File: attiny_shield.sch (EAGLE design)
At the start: 10 parts, among them IC1 TINY13-20PU

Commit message: reset pins won't need to be set manually
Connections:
- removed net 84_RESET: J3.4, U$1.(PCINT11/~RESET/DW)PB3
- removed net 85_RESET: IC1.PB5/PCINT5/!RESET!/ADC0/DW, J4.1
- removed net RESET: U$2.D10
- new net TINY_RESET: IC1.PB5/PCINT5/!RESET!/ADC0/DW, J3.4, J4.1, U$1.(PCINT11/~RESET/DW)PB3, U$2.D10
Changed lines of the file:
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@@
 </segment>
 </net>
-<net name="RESET" class="0">
+<net name="TINY_RESET" class="0">
 <segment>
 <pinref part="U$2" gate="G$1" pin="D10"/>
 <wire x1="55.88" y1="147.32" x2="55.88" y2="152.4" width="0.1524" layer="91"/>
 <label x="55.88" y="149.86" size="1.778" layer="95"/>
+</segment>
+<segment>
+<pinref part="J4" gate="G$1" pin="1"/>
+<wire x1="144.78" y1="91.44" x2="134.62" y2="91.44" width="0.1524" layer="91"/>
+<label x="134.62" y="91.44" size="1.778" layer="95"/>
+</segment>
+<segment>
+<pinref part="IC1" gate="G$1" pin="PB5/PCINT5/!RESET!/ADC0/DW"/>
+<wire x1="121.92" y1="109.22" x2="147.32" y2="109.22" width="0.1524" layer="91"/>
+<label x="121.92" y="109.22" size="1.778" layer="95"/>
+</segment>
+<segment>
+<pinref part="J3" gate="G$1" pin="4"/>
+<wire x1="63.5" y1="22.86" x2="53.34" y2="22.86" width="0.1524" layer="91"/>
+<label x="53.34" y="22.86" size="1.778" layer="95"/>
+</segment>
+<segment>
+<pinref part="U$1" gate="G$1" pin="(PCINT11/~RESET/DW)PB3"/>
+<wire x1="30.48" y1="66.04" x2="20.32" y2="66.04" width="0.1524" layer="91"/>
+<label x="22.86" y="66.04" size="1.778" layer="95"/>
 </segment>
 </net>
@@
 </segment>
 </net>
-<net name="84_RESET" class="0">
-<segment>
-<pinref part="J3" gate="G$1" pin="4"/>
-<wire x1="63.5" y1="22.86" x2="53.34" y2="22.86" width="0.1524" layer="91"/>
-<label x="53.34" y="22.86" size="1.778" layer="95"/>
-</segment>
-<segment>
-<pinref part="U$1" gate="G$1" pin="(PCINT11/~RESET/DW)PB3"/>
-<wire x1="30.48" y1="66.04" x2="20.32" y2="66.04" width="0.1524" layer="91"/>
-<label x="22.86" y="66.04" size="1.778" layer="95"/>
-</segment>
-</net>
-<net name="85_RESET" class="0">
-<segment>
-<pinref part="J4" gate="G$1" pin="1"/>
-<wire x1="144.78" y1="91.44" x2="134.62" y2="91.44" width="0.1524" layer="91"/>
-<label x="134.62" y="91.44" size="1.778" layer="95"/>
-</segment>
-<segment>
-<pinref part="IC1" gate="G$1" pin="PB5/PCINT5/!RESET!/ADC0/DW"/>
-<wire x1="121.92" y1="109.22" x2="147.32" y2="109.22" width="0.1524" layer="91"/>
-<label x="121.92" y="109.22" size="1.778" layer="95"/>
-</segment>
-</net>

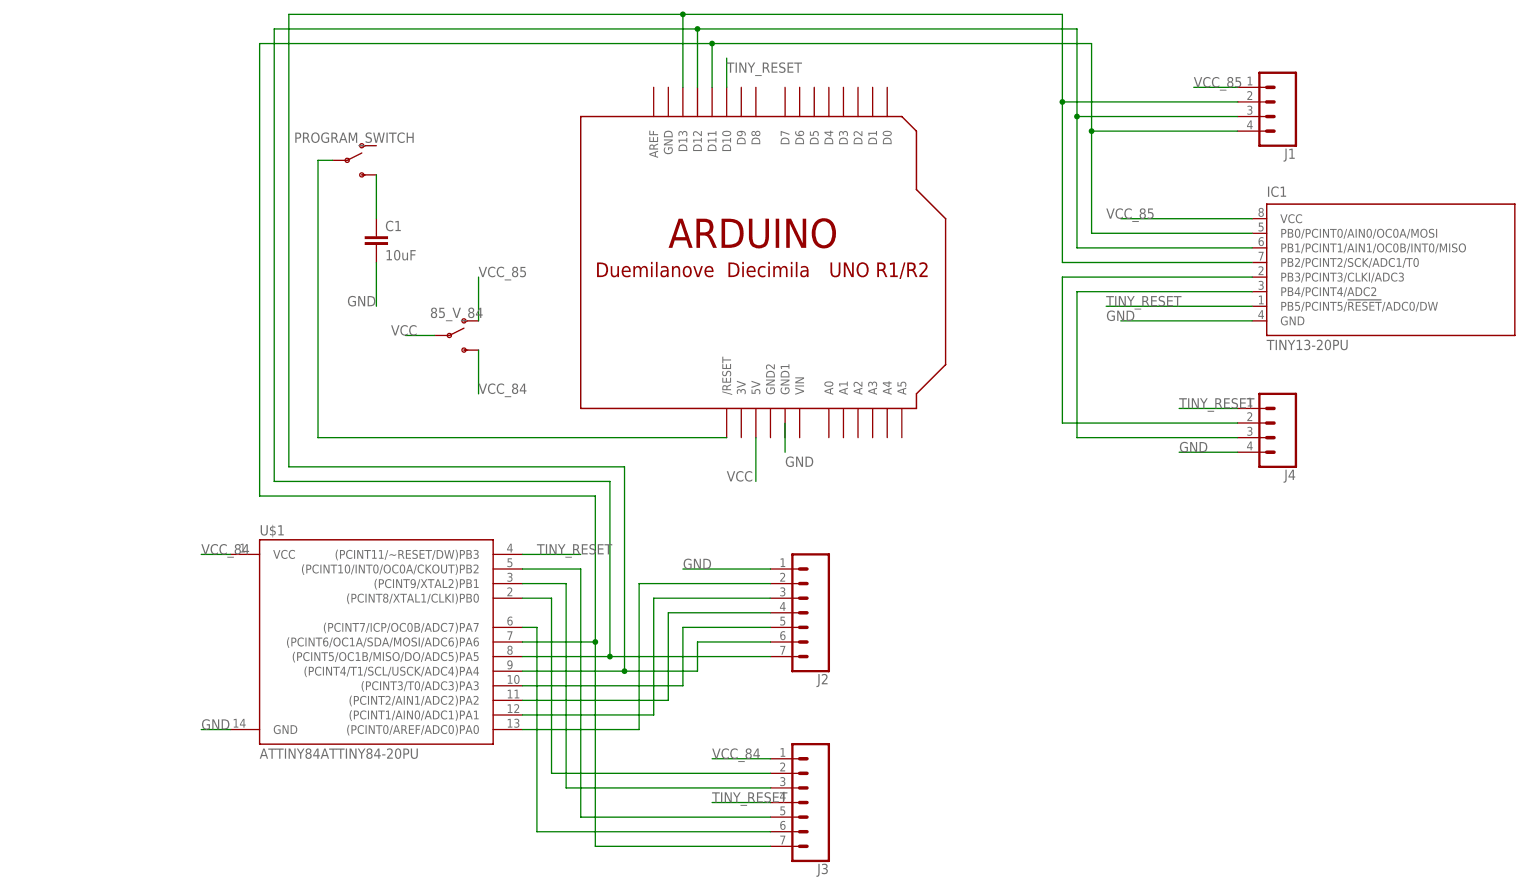
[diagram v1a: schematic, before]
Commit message: reset not vcc
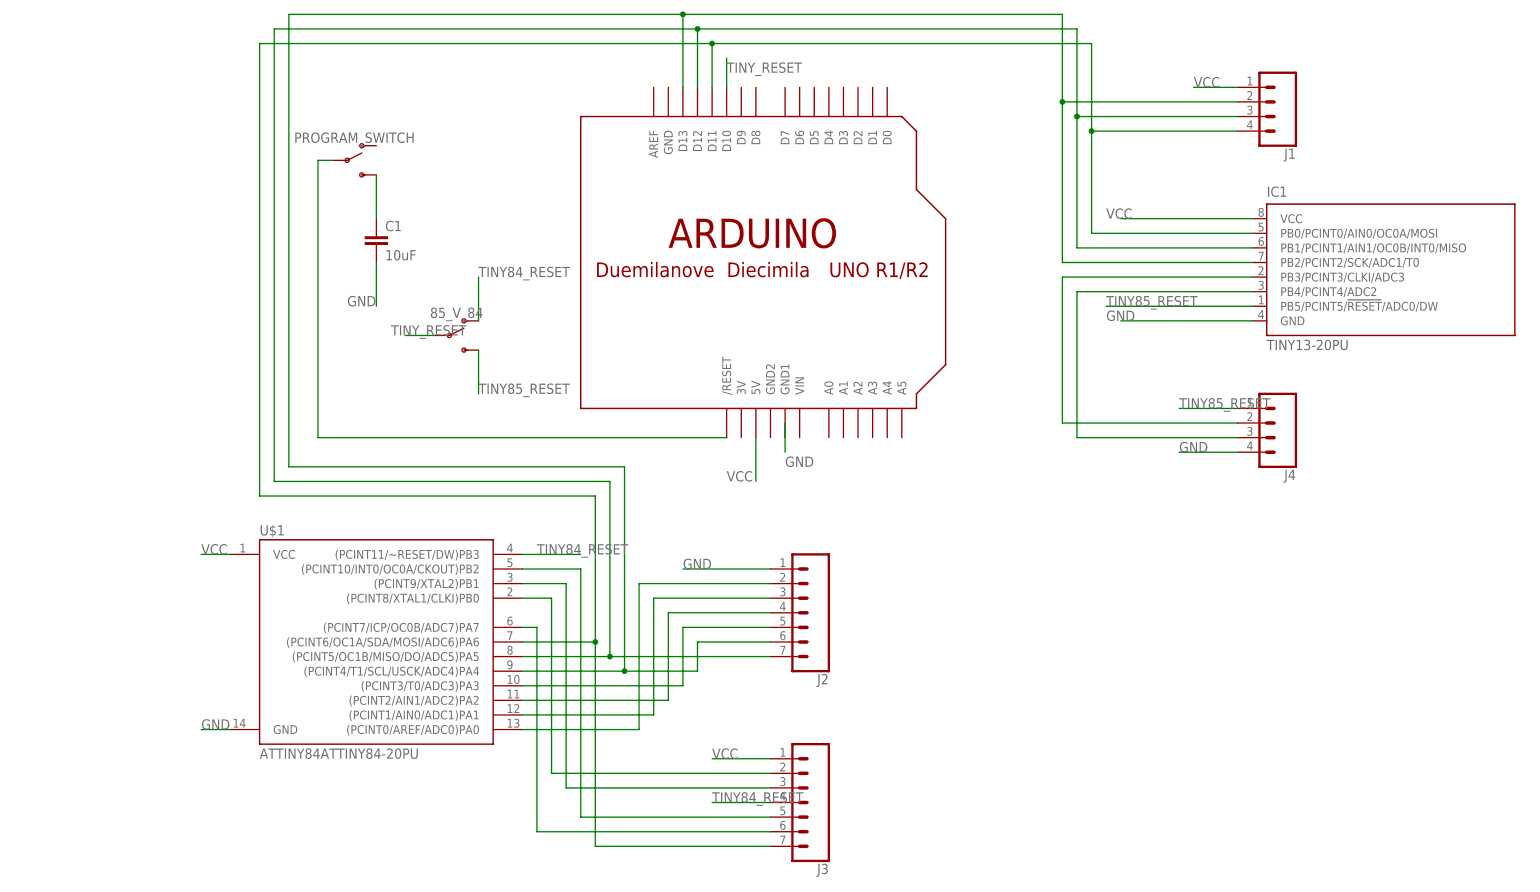
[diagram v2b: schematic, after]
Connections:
- removed net VCC_84: 85_V_84.S, J3.1, U$1.VCC
- removed net VCC_85: 85_V_84.O, IC1.VCC, J1.1
- new net TINY84_RESET: 85_V_84.O, J3.4, U$1.(PCINT11/~RESET/DW)PB3
- new net TINY85_RESET: 85_V_84.S, IC1.PB5/PCINT5/!RESET!/ADC0/DW, J4.1
- net TINY_RESET: now also 85_V_84.P; no longer IC1.PB5/PCINT5/!RESET!/ADC0/DW, J3.4, J4.1, U$1.(PCINT11/~RESET/DW)PB3
- net VCC: now also IC1.VCC, J1.1, J3.1, U$1.VCC; no longer 85_V_84.P
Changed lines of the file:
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@@
 </segment>
 <segment>
-<pinref part="J4" gate="G$1" pin="1"/>
-<wire x1="144.78" y1="91.44" x2="134.62" y2="91.44" width="0.1524" layer="91"/>
-<label x="134.62" y="91.44" size="1.778" layer="95"/>
-</segment>
-<segment>
-<pinref part="IC1" gate="G$1" pin="PB5/PCINT5/!RESET!/ADC0/DW"/>
-<wire x1="121.92" y1="109.22" x2="147.32" y2="109.22" width="0.1524" layer="91"/>
-<label x="121.92" y="109.22" size="1.778" layer="95"/>
-</segment>
-<segment>
-<pinref part="J3" gate="G$1" pin="4"/>
-<wire x1="63.5" y1="22.86" x2="53.34" y2="22.86" width="0.1524" layer="91"/>
-<label x="53.34" y="22.86" size="1.778" layer="95"/>
-</segment>
-<segment>
-<pinref part="U$1" gate="G$1" pin="(PCINT11/~RESET/DW)PB3"/>
-<wire x1="30.48" y1="66.04" x2="20.32" y2="66.04" width="0.1524" layer="91"/>
-<label x="22.86" y="66.04" size="1.778" layer="95"/>
-</segment>
-</net>
-<net name="VCC_85" class="0">
-<segment>
-<pinref part="85_V_84" gate="1" pin="O"/>
-<wire x1="12.7" y1="106.68" x2="12.7" y2="114.3" width="0.1524" layer="91"/>
-<label x="12.7" y="114.3" size="1.778" layer="95"/>
-</segment>
-<segment>
-<pinref part="IC1" gate="G$1" pin="VCC"/>
-<wire x1="147.32" y1="124.46" x2="124.46" y2="124.46" width="0.1524" layer="91"/>
-<label x="121.92" y="124.46" size="1.778" layer="95"/>
-</segment>
-<segment>
-<pinref part="J1" gate="G$1" pin="1"/>
-<wire x1="144.78" y1="147.32" x2="137.16" y2="147.32" width="0.1524" layer="91"/>
-<label x="137.16" y="147.32" size="1.778" layer="95"/>
+<pinref part="85_V_84" gate="1" pin="P"/>
+<wire x1="5.08" y1="104.14" x2="0" y2="104.14" width="0.1524" layer="91"/>
+<label x="-2.54" y="104.14" size="1.778" layer="95"/>
 </segment>
 </net>
@@
 </segment>
 <segment>
-<pinref part="85_V_84" gate="1" pin="P"/>
-<wire x1="5.08" y1="104.14" x2="0" y2="104.14" width="0.1524" layer="91"/>
-<label x="-2.54" y="104.14" size="1.778" layer="95"/>
-</segment>
-</net>
-<net name="VCC_84" class="0">
-<segment>
 <pinref part="U$1" gate="G$1" pin="VCC"/>
 <wire x1="-35.56" y1="66.04" x2="-30.48" y2="66.04" width="0.1524" layer="91"/>
@@
 </segment>
 <segment>
-<pinref part="85_V_84" gate="1" pin="S"/>
-<wire x1="12.7" y1="101.6" x2="12.7" y2="93.98" width="0.1524" layer="91"/>
-<label x="12.7" y="93.98" size="1.778" layer="95"/>
-</segment>
-<segment>
 <pinref part="J3" gate="G$1" pin="1"/>
 <wire x1="63.5" y1="30.48" x2="53.34" y2="30.48" width="0.1524" layer="91"/>
 <label x="53.34" y="30.48" size="1.778" layer="95"/>
+</segment>
+<segment>
+<pinref part="IC1" gate="G$1" pin="VCC"/>
+<wire x1="147.32" y1="124.46" x2="124.46" y2="124.46" width="0.1524" layer="91"/>
+<label x="121.92" y="124.46" size="1.778" layer="95"/>
+</segment>
+<segment>
+<pinref part="J1" gate="G$1" pin="1"/>
+<wire x1="144.78" y1="147.32" x2="137.16" y2="147.32" width="0.1524" layer="91"/>
+<label x="137.16" y="147.32" size="1.778" layer="95"/>
 </segment>
 </net>
@@
 </segment>
 </net>
+<net name="TINY85_RESET" class="0">
+<segment>
+<pinref part="IC1" gate="G$1" pin="PB5/PCINT5/!RESET!/ADC0/DW"/>
+<wire x1="121.92" y1="109.22" x2="147.32" y2="109.22" width="0.1524" layer="91"/>
+<label x="121.92" y="109.22" size="1.778" layer="95"/>
+</segment>
+<segment>
+<pinref part="J4" gate="G$1" pin="1"/>
+<wire x1="144.78" y1="91.44" x2="134.62" y2="91.44" width="0.1524" layer="91"/>
+<label x="134.62" y="91.44" size="1.778" layer="95"/>
+</segment>
+<segment>
+<pinref part="85_V_84" gate="1" pin="S"/>
+<wire x1="12.7" y1="101.6" x2="12.7" y2="93.98" width="0.1524" layer="91"/>
+<label x="12.7" y="93.98" size="1.778" layer="95"/>
+</segment>
+</net>
+<net name="TINY84_RESET" class="0">
+<segment>
+<pinref part="J3" gate="G$1" pin="4"/>
+<wire x1="63.5" y1="22.86" x2="53.34" y2="22.86" width="0.1524" layer="91"/>
+<label x="53.34" y="22.86" size="1.778" layer="95"/>
+</segment>
+<segment>
+<pinref part="U$1" gate="G$1" pin="(PCINT11/~RESET/DW)PB3"/>
+<wire x1="30.48" y1="66.04" x2="20.32" y2="66.04" width="0.1524" layer="91"/>
+<label x="22.86" y="66.04" size="1.778" layer="95"/>
+</segment>
+<segment>
+<pinref part="85_V_84" gate="1" pin="O"/>
+<wire x1="12.7" y1="106.68" x2="12.7" y2="114.3" width="0.1524" layer="91"/>
+<label x="12.7" y="114.3" size="1.778" layer="95"/>
+</segment>
+</net>

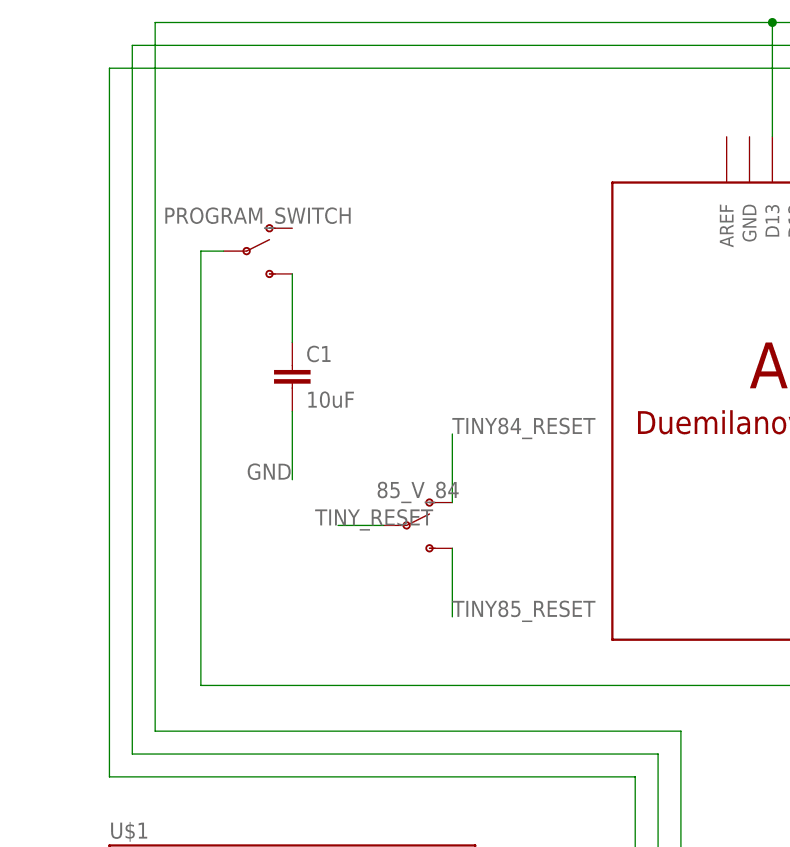
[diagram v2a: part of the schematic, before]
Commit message: added reset switch
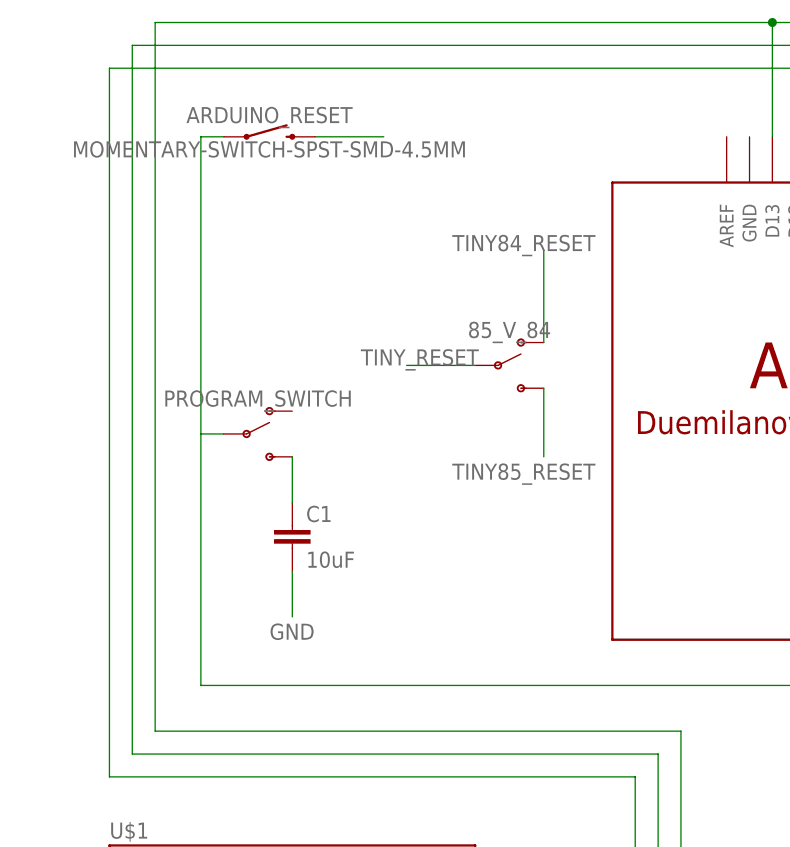
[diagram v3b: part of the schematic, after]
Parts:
- added ARDUINO_RESET: MOMENTARY-SWITCH-SPST-SMD-4.5MM, SparkFun-Switches:MOMENTARY-SWITCH-SPST-SMD-4.5MM
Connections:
- net GND: now also ARDUINO_RESET.2
- net N$10: now also ARDUINO_RESET.1
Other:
- moved on the sheet: 85_V_84, C1, PROGRAM_SWITCH
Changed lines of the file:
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@@
 <part name="J4" library="SparkFun-Connectors" deviceset="CONN_04" device=""/>
 <part name="C1" library="SparkFun-Capacitors" deviceset="10UF" device="-0805-10V-10%" value="10uF"/>
+<part name="ARDUINO_RESET" library="SparkFun-Switches" deviceset="MOMENTARY-SWITCH-SPST" device="-SMD-4.5MM"/>
 </parts>
 <sheets>
@@
 <instance part="IC1" gate="G$1" x="167.64" y="111.76"/>
 <instance part="U$2" gate="G$1" x="53.34" y="119.38"/>
-<instance part="PROGRAM_SWITCH" gate="1" x="-10.16" y="134.62"/>
-<instance part="85_V_84" gate="1" x="7.62" y="104.14"/>
+<instance part="PROGRAM_SWITCH" gate="1" x="-10.16" y="114.3"/>
+<instance part="85_V_84" gate="1" x="17.78" y="121.92"/>
 <instance part="J2" gate="G$1" x="68.58" y="58.42" rot="R180"/>
 <instance part="J3" gate="G$1" x="68.58" y="25.4" rot="R180"/>
 <instance part="J1" gate="G$1" x="149.86" y="144.78" rot="R180"/>
 <instance part="J4" gate="G$1" x="149.86" y="88.9" rot="R180"/>
-<instance part="C1" gate="G$1" x="-5.08" y="119.38"/>
+<instance part="C1" gate="G$1" x="-5.08" y="101.6"/>
+<instance part="ARDUINO_RESET" gate="G$1" x="-7.62" y="147.32"/>
 </instances>
 <busses>
@@
 <segment>
 <pinref part="85_V_84" gate="1" pin="P"/>
-<wire x1="5.08" y1="104.14" x2="0" y2="104.14" width="0.1524" layer="91"/>
-<label x="-2.54" y="104.14" size="1.778" layer="95"/>
+<wire x1="15.24" y1="121.92" x2="7.62" y2="121.92" width="0.1524" layer="91"/>
+<label x="2.54" y="121.92" size="1.778" layer="95"/>
 </segment>
 </net>
@@
 <segment>
 <pinref part="PROGRAM_SWITCH" gate="1" pin="S"/>
-<wire x1="-5.08" y1="132.08" x2="-5.08" y2="124.46" width="0.1524" layer="91"/>
+<wire x1="-5.08" y1="111.76" x2="-5.08" y2="106.68" width="0.1524" layer="91"/>
 <pinref part="C1" gate="G$1" pin="1"/>
 </segment>
@@
 <pinref part="PROGRAM_SWITCH" gate="1" pin="P"/>
 <pinref part="U$2" gate="G$1" pin="/RESET"/>
-<wire x1="-12.7" y1="134.62" x2="-15.24" y2="134.62" width="0.1524" layer="91"/>
-<wire x1="-15.24" y1="134.62" x2="-15.24" y2="86.36" width="0.1524" layer="91"/>
+<wire x1="-12.7" y1="114.3" x2="-15.24" y2="114.3" width="0.1524" layer="91"/>
+<wire x1="-15.24" y1="114.3" x2="-15.24" y2="86.36" width="0.1524" layer="91"/>
 <wire x1="-15.24" y1="86.36" x2="55.88" y2="86.36" width="0.1524" layer="91"/>
+<wire x1="-15.24" y1="114.3" x2="-15.24" y2="147.32" width="0.1524" layer="91"/>
+<pinref part="ARDUINO_RESET" gate="G$1" pin="1"/>
+<wire x1="-15.24" y1="147.32" x2="-12.7" y2="147.32" width="0.1524" layer="91"/>
 </segment>
 </net>
@@
 </segment>
 <segment>
-<wire x1="-5.08" y1="116.84" x2="-5.08" y2="109.22" width="0.1524" layer="91"/>
-<label x="-10.16" y="109.22" size="1.778" layer="95"/>
+<wire x1="-5.08" y1="99.06" x2="-5.08" y2="93.98" width="0.1524" layer="91"/>
+<label x="-7.62" y="91.44" size="1.778" layer="95"/>
 <pinref part="C1" gate="G$1" pin="2"/>
 </segment>
@@
 <wire x1="144.78" y1="83.82" x2="134.62" y2="83.82" width="0.1524" layer="91"/>
 <label x="134.62" y="83.82" size="1.778" layer="95"/>
+</segment>
+<segment>
+<pinref part="ARDUINO_RESET" gate="G$1" pin="2"/>
+<wire x1="-2.54" y1="147.32" x2="5.08" y2="147.32" width="0.1524" layer="91"/>
 </segment>
 </net>
@@
 <segment>
 <pinref part="85_V_84" gate="1" pin="S"/>
-<wire x1="12.7" y1="101.6" x2="12.7" y2="93.98" width="0.1524" layer="91"/>
-<label x="12.7" y="93.98" size="1.778" layer="95"/>
+<wire x1="22.86" y1="119.38" x2="22.86" y2="111.76" width="0.1524" layer="91"/>
+<label x="12.7" y="109.22" size="1.778" layer="95"/>
 </segment>
 </net>
@@
 <segment>
 <pinref part="85_V_84" gate="1" pin="O"/>
-<wire x1="12.7" y1="106.68" x2="12.7" y2="114.3" width="0.1524" layer="91"/>
-<label x="12.7" y="114.3" size="1.778" layer="95"/>
-</segment>
-</net>
+<wire x1="22.86" y1="124.46" x2="22.86" y2="134.62" width="0.1524" layer="91"/>
+<label x="12.7" y="134.62" size="1.778" layer="95"/>
+</segment>
+</net>
